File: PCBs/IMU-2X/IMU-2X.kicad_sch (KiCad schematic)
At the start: 62 parts, among them J1 CAN-FD, J2 Power, J3 USB_B, J4 CAN-FD, J5 SWD, Q1 DMP2004K-7, SW1 RESET, SW2 BOOT0, U1 MCP2542FDT-E/SN, U10 IAM-20680HP, U2 USBLC6-2SC6, U4 SCHA63T-K03, U5 8MHz-ECS-5032MV, U6 STM32G473RET6, U7 MCP120T-270I/TT, U9 SN74AVC4T245DR

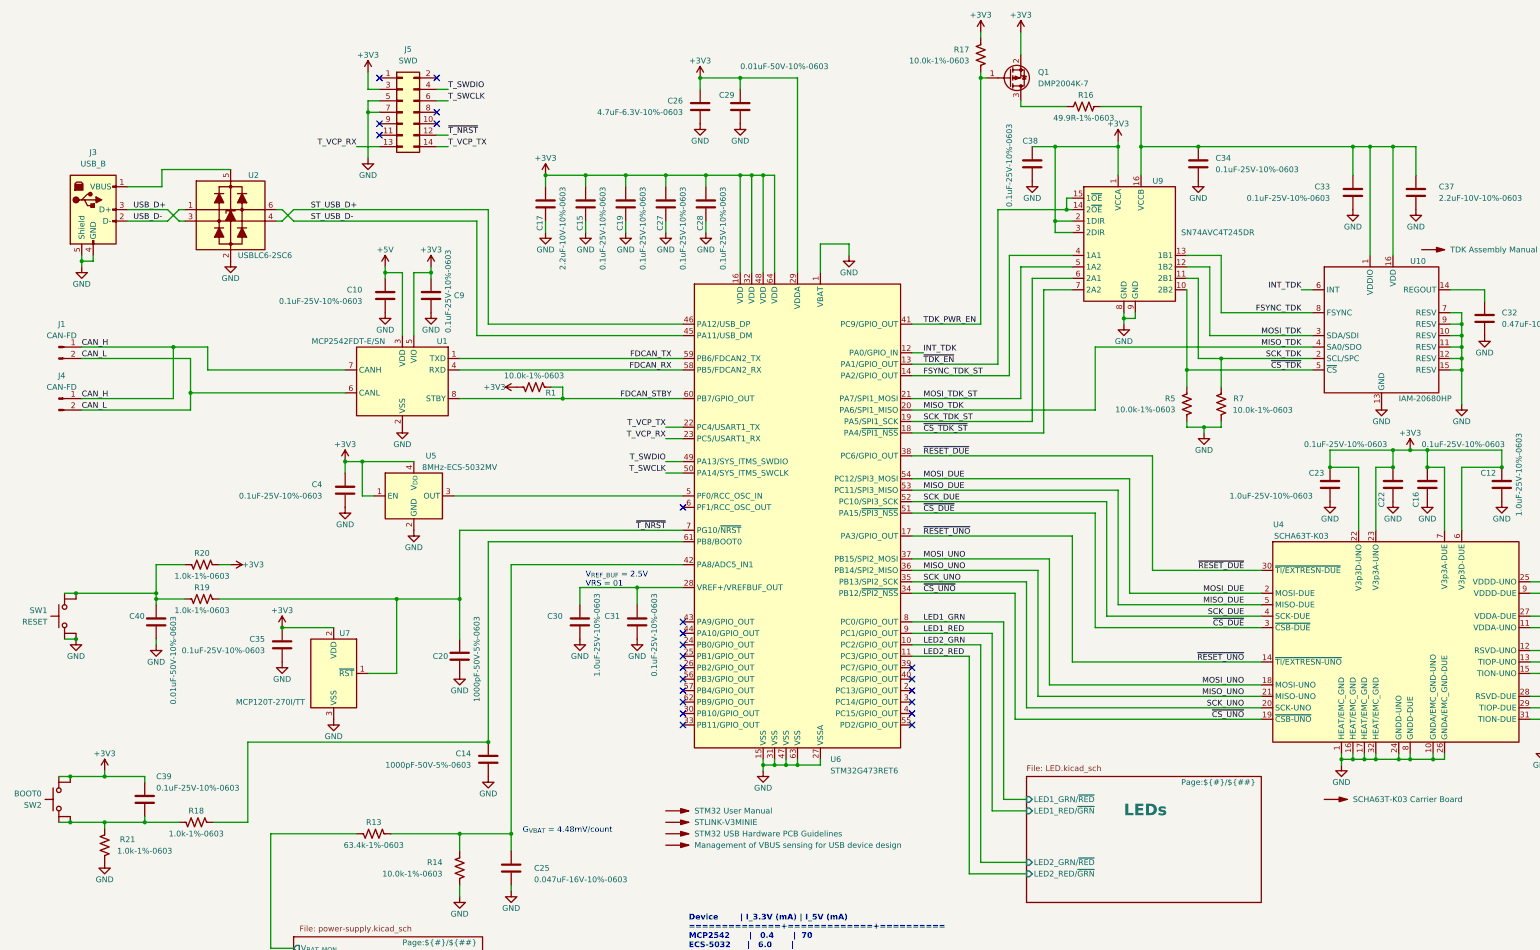
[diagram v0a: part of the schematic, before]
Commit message: Adding IMU-2X-v2 fixes switch footprint.
Signed-off-by: Scott <sgberman1@gmail.com>
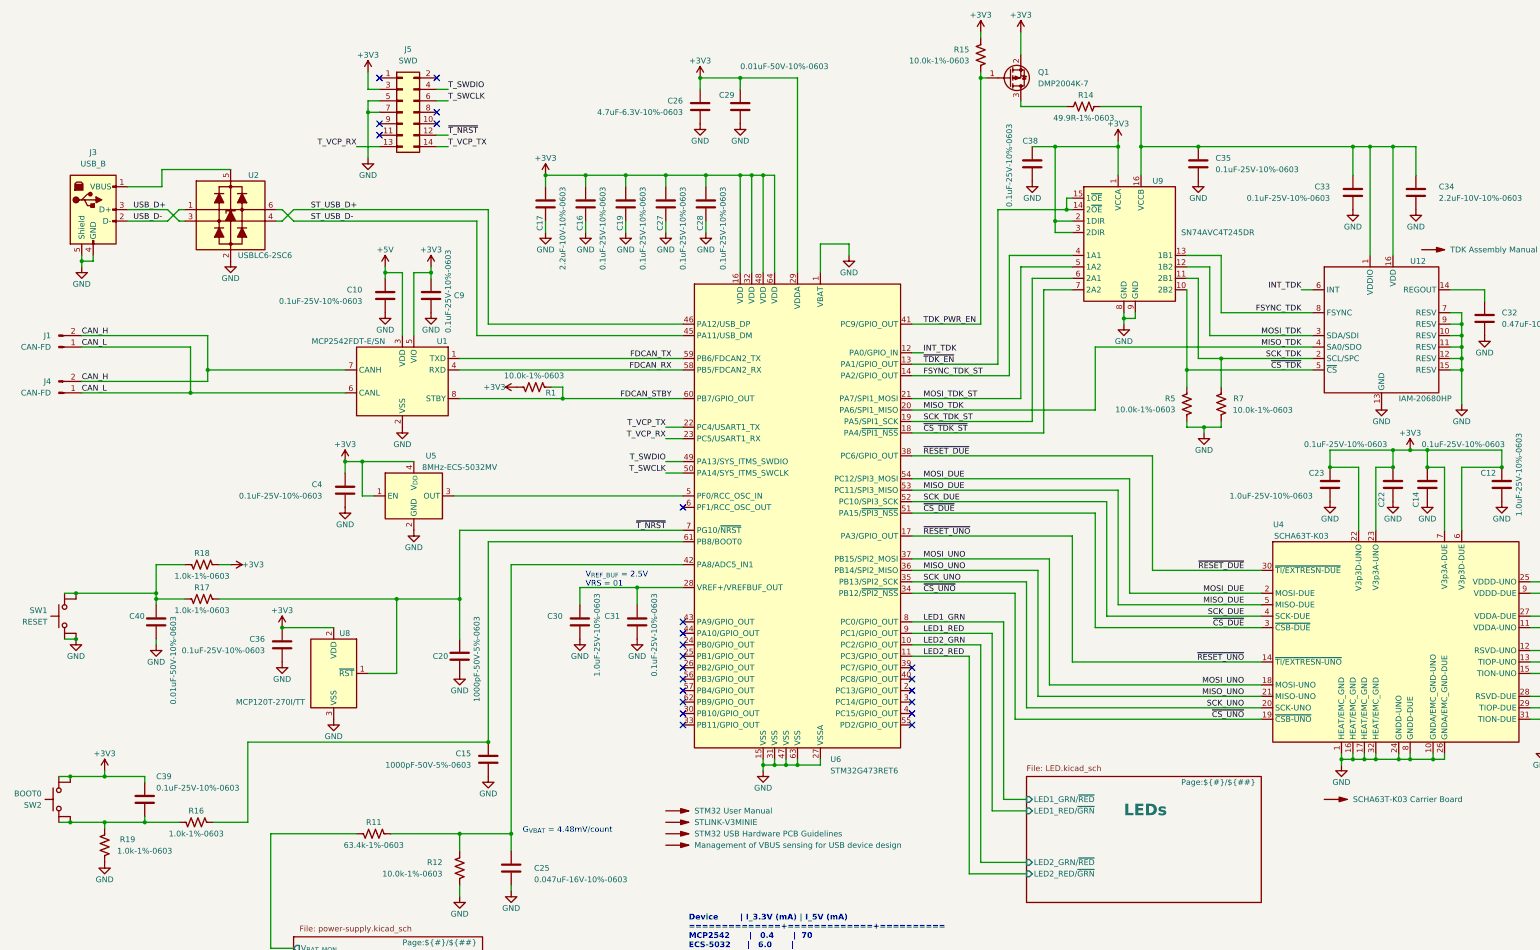
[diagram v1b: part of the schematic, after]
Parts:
- J1, J4: DIST P/N WM4800-ND -> WM14047-ND; MFG P/N 0705430001 -> 0705410001
- renumbered C16 to C14, C14 to C15, C15 to C16, C37 to C34, C34 to C35, C35 to C36, R13 to R11, R14 to R12, R16 to R14, R17 to R15, R18 to R16, R19 to R17, R20 to R18, R21 to R19, U10 to U12, U7 to U8
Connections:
- net +3V3: now also SW2.2; no longer SW2.3
- net CAN_H: now also J1.2 (Pin_2), J4.2 (Pin_2); no longer J1.1 (Pin_1), J4.1 (Pin_1)
- net CAN_L: now also J1.1 (Pin_1), J4.1 (Pin_1); no longer J1.2 (Pin_2), J4.2 (Pin_2)
- net GND: now also SW1.2; no longer SW1.3
- net at C39.2, R16.1, R19.1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: now also SW2.3; no longer SW2.2
- net at C40.1, R17.1, R18.1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: now also SW1.3; no longer SW1.2
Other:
- moved on the sheet: J1, J4
